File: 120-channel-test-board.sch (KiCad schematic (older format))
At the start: 258 parts, among them P1 CONN_01X01, P10 CONN_01X01, P100 CONN_01X01, P101 CONN_01X01, P102 CONN_01X01, P103 CONN_01X01, P104 CONN_01X01, P105 CONN_01X01, P106 CONN_01X01, P107 CONN_01X01, P108 CONN_01X01, P109 CONN_01X01, P11 CONN_01X01, P110 CONN_01X01, P111 CONN_01X01, P112 CONN_01X01, P113 CONN_01X01, P114 CONN_01X01, P115 CONN_01X01, P116 CONN_01X01, P117 CONN_01X01, P118 CONN_01X01, P119 CONN_01X01, P12 CONN_01X01, P120 CONN_01X01, P121 CONN_01X01, P122 CONN_01X01, P123 CONN_01X01, P124 CONN_01X01, P125 CONN_01X01, P126 CONN_01X01, P127 CONN_01X01, P128 CONN_01X01, P129 CONN_01X01, P13 CONN_01X01, P130 CONN_01X01, P131 CONN_01X01, P132 CONN_01X01, P133 CONN_01X01, P134 CONN_01X01, P135 CONN_01X01, P136 CONN_01X01, P137 CONN_01X01, P138 CONN_01X01, P14 CONN_01X01, P15 CONN_01X01, P16 CONN_01X01, P17 CONN_01X01, P18 CONN_01X01, P19 CONN_01X01, P2 CONN_01X01, P20 CONN_01X01, P21 CONN_01X01, P22 CONN_01X01, P23 CONN_01X01, P24 CONN_01X01, P25 CONN_01X01, P26 CONN_01X01, P27 CONN_01X01, P28 CONN_01X01, P29 CONN_01X01, P3 CONN_01X01, P30 CONN_01X01, P31 CONN_01X01, P32 CONN_01X01, P33 CONN_01X01, P34 CONN_01X01, P35 CONN_01X01, P36 CONN_01X01, P37 CONN_01X01, P38 CONN_01X01, P39 CONN_01X01, P4 CONN_01X01, P40 CONN_01X01, P41 CONN_01X01, P42 CONN_01X01, P43 CONN_01X01, P44 CONN_01X01, P45 CONN_01X01, P46 CONN_01X01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

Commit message: Update for KiCad 5 and reorganize folders
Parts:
- C1, C10, C100, C101, C102, C103, C104, C105, C106, C107, C108, C109, C11, C110, C111, C112, C113, C114, C115, C116, C117, C118, C119, C12, C120, C13, C14, C15, C16, C17, C18, C19, C2, C20, C21, C22, C23, C24, C25, C26, C27, C28, C29, C3, C30, C31, C32, C33, C34, C35, C36, C37, C38, C39, C4, C40, C41, C42, C43, C44, C45, C46, C47, C48, C49, C5, C50, C51, C52, C53, C54, C55, C56, C57, C58, C59, C6, C60, C61, C62, C63, C64, C65, C66, C67, C68, C69, C7, C70, C71, C72, C73, C74, C75, C76, C77, C78, C79, C8, C80, C81, C82, C83, C84, C85, C86, C87, C88, C89, C9, C90, C91, C92, C93, C94, C95, C96, C97, C98, C99: symbol C -> Device:C; MPN (none) -> CC1206JKNPOCBN100; Manufacturer (none) -> YAGEO
- P1, P10, P100, P101, P102, P103, P104, P105, P106, P107, P108, P109, P11, P110, P111, P112, P113, P114, P115, P116, P117, P118, P119, P12, P120, P121, P122, P123, P124, P125, P126, P127, P128, P129, P13, P130, P131, P132, P133, P134, P135, P136, P137, P138, P14, P15, P16, P17, P18, P19, P2, P20, P21, P22, P23, P24, P25, P26, P27, P28, P29, P3, P30, P31, P32, P33, P34, P35, P36, P37, P38, P39, P4, P40, P41, P42, P43, P44, P45, P46, P47, P48, P49, P5, P50, P51, P52, P53, P54, P55, P56, P57, P58, P59, P6, P60, P61, P62, P63, P64, P65, P66, P67, P68, P69, P7, P70, P71, P72, P73, P74, P75, P76, P77, P78, P79, P8, P80, P81, P82, P83, P84, P85, P86, P87, P88, P89, P9, P90, P91, P92, P93, P94, P95, P96, P97, P98, P99: symbol Conn_01x01 -> Connector_Generic:Conn_01x01
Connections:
- net CUR_SENSE: no longer P121.1 (Pin_1), P123.1 (Pin_1), P124.1 (Pin_1), P138.1 (Pin_1)

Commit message: Update kicad_helpers
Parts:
- P1, P10, P100, P101, P102, P103, P104, P105, P106, P107, P108, P109, P11, P110, P111, P112, P113, P114, P115, P116, P117, P118, P119, P12, P120, P122, P123, P124, P125, P126, P127, P128, P129, P13, P130, P131, P132, P133, P134, P135, P136, P137, P14, P15, P16, P17, P18, P19, P2, P20, P21, P22, P23, P24, P25, P26, P27, P28, P29, P3, P30, P31, P32, P33, P34, P35, P36, P37, P38, P39, P4, P40, P41, P42, P43, P44, P45, P46, P47, P48, P49, P5, P50, P51, P52, P53, P54, P55, P56, P57, P58, P59, P6, P60, P61, P62, P63, P64, P65, P66, P67, P68, P69, P7, P70, P71, P72, P73, P74, P75, P76, P77, P78, P79, P8, P80, P81, P82, P83, P84, P85, P86, P87, P88, P89, P9, P90, P91, P92, P93, P94, P95, P96, P97, P98, P99: footprint wheelerlab:1.9mm_DMF_Electrode -> Sci-Bots:1.9mm_DMF_Electrode; MPN (none) -> DNP; Manufacturer (none) -> DNP
- P121, P138: MPN (none) -> DNP; Manufacturer (none) -> DNP

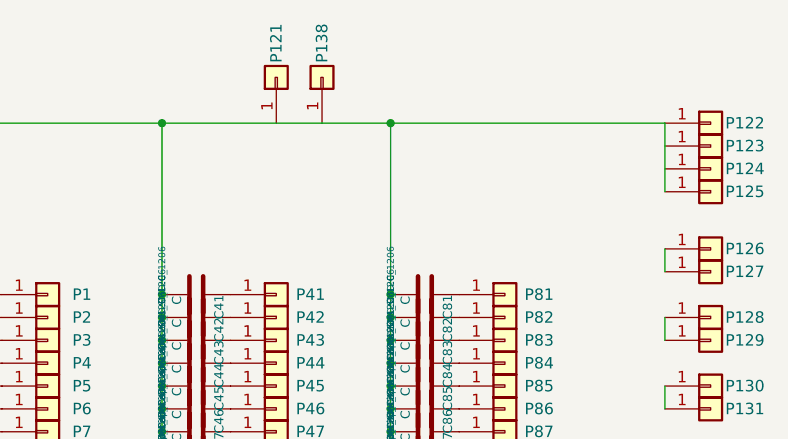
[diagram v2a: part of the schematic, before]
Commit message: Fix some ERC errors
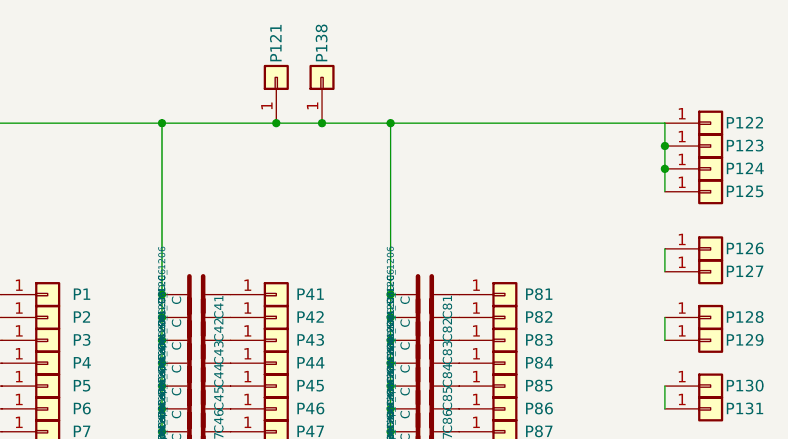
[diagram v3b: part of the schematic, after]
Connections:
- net CUR_SENSE: now also P121.1 (Pin_1), P123.1 (Pin_1), P124.1 (Pin_1), P138.1 (Pin_1)
